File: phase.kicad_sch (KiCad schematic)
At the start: 19 parts

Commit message: finished schematics
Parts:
- removed U?: BSC040N08, Package_TO_SOT_SMD:LFPAK56_ThermalVias-1, symbol Transistor_FET:BSC040N08NS5
- removed U?: 22R, Resistor_SMD:R_0603_1608Metric, symbol Device:R
- removed U?: 0mr5, Resistor_SMD:R_2512_6332Metric, symbol Device:R
- removed U?: 10u, Capacitor_SMD:C_2220_5650Metric, symbol Device:C
- added C39: 10u, Capacitor_SMD:C_2220_5650Metric, symbol Device:C
- added Q24: BSC040N08, Package_TO_SOT_SMD:TDSON-8-1, symbol Transistor_FET:BSC040N08NS5
- added R31: 22R, Resistor_SMD:R_0603_1608Metric, symbol Device:R
- added R34: 0mr5, Resistor_SMD:R_2512_6332Metric, symbol Device:R
- Q23: renamed from U?; footprint Package_TO_SOT_SMD:LFPAK56_ThermalVias-1 -> Package_TO_SOT_SMD:TDSON-8-1
- gave numbers to parts that had none: 14
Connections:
- net GND is gone; now on net GNDA: C40.2, U25.1 (GND), U25.4 (GND), U25.7 (REF1)
- net +BATT: now also C39.1
- net GNDPWR: now also C39.2, Q24.1 (S), Q24.2 (S), Q24.3 (S)
- net Phase: now also R34.1
- net at C34.2, C35.2, Q23.1 (S)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: now also R32.1, Q24.5 (D), R34.2
- net at U24.5 (LO): now also R31.2
- net V: now reaches C36.1, R32.2, R33.1
- net +3.3VA renamed +3.3VADC
- new net: Q24.4 (G), R31.1
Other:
- company: (none) -> UNIMOC universal motor controller
- title: Phase -> (BCC) Battery Case Controller

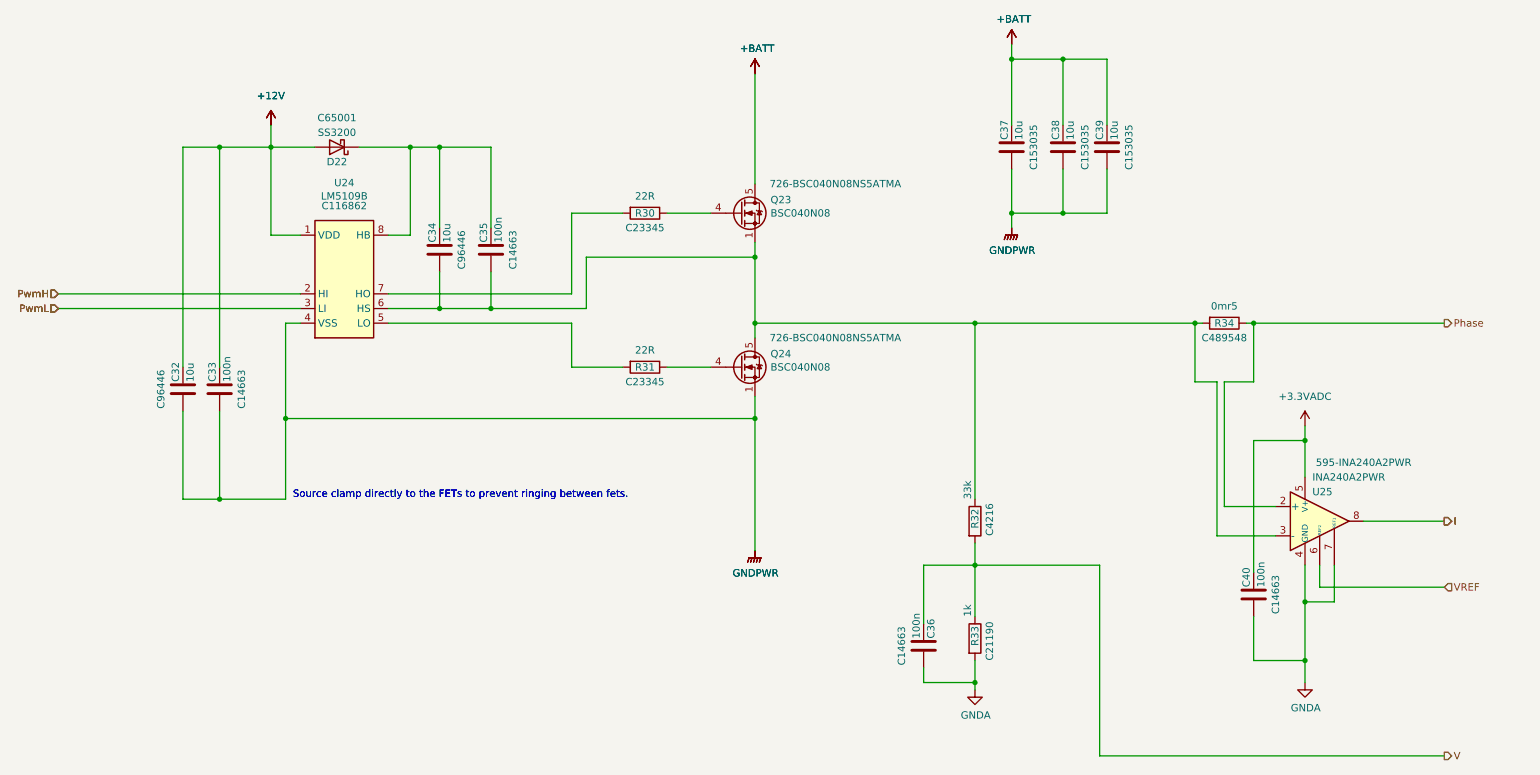
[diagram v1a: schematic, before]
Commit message: Placing first round finished
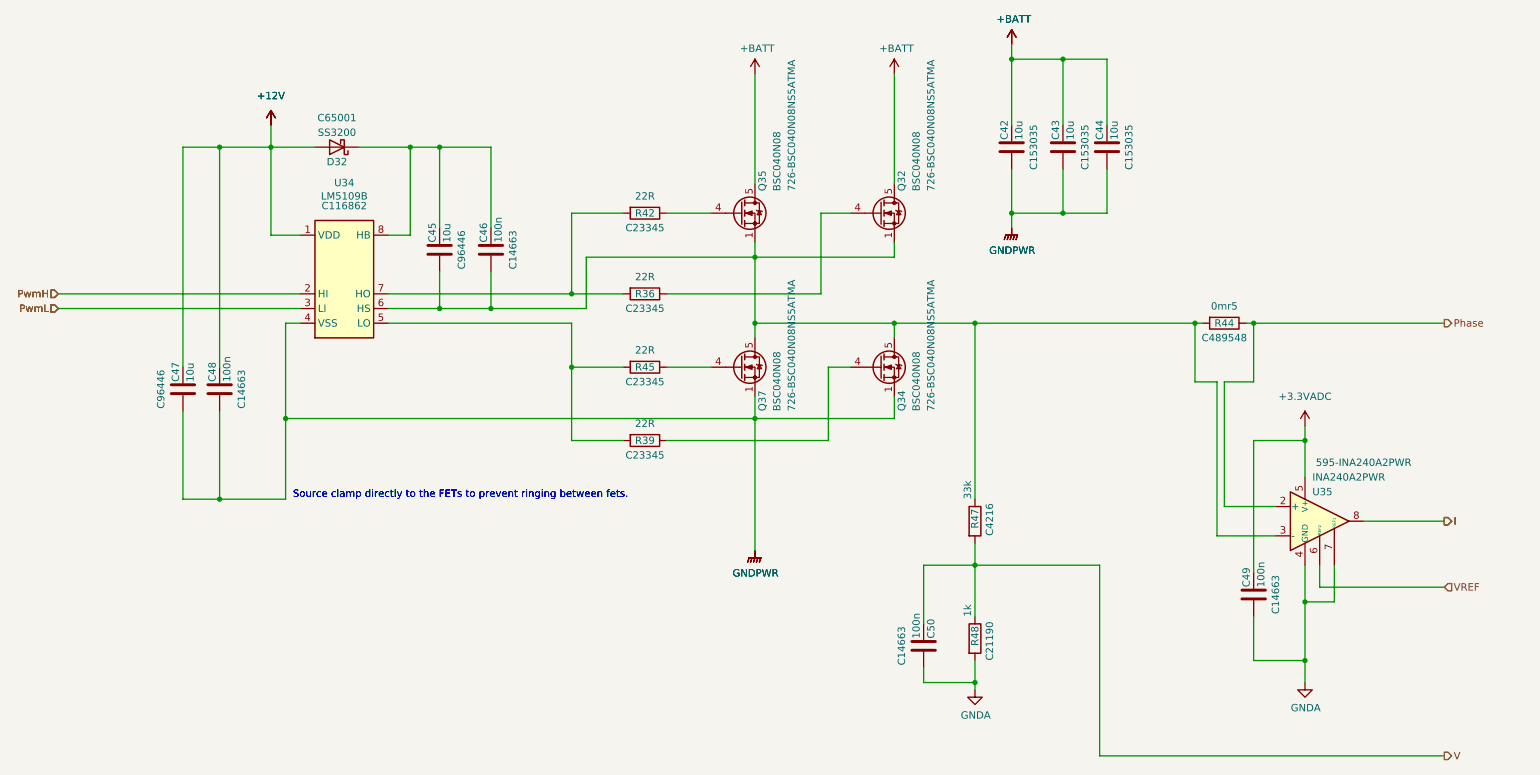
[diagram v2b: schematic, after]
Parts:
- added Q32, Q34: BSC040N08, Package_TO_SOT_SMD:TDSON-8-1, symbol Transistor_FET:BSC040N08NS5
- added R36, R39: 22R, Resistor_SMD:R_0603_1608Metric, symbol Device:R
- renumbered C37 to C42, C38 to C43, C39 to C44, C34 to C45, C35 to C46, C32 to C47, C33 to C48, C40 to C49, C36 to C50, D22 to D32, Q23 to Q35, Q24 to Q37, R30 to R42, R34 to R44, R31 to R45, R32 to R47, R33 to R48, U24 to U34, U25 to U35
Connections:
- net +BATT: now also Q32.5 (D)
- net GNDPWR: now also Q34.1 (S), Q34.2 (S), Q34.3 (S)
- net at C45.2, C46.2, Q35.1 (S)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: now also Q32.1 (S), Q32.2 (S), Q32.3 (S), Q34.5 (D)
- net at R42.2, U34.7 (HO): now also R36.2
- net at R45.2, U34.5 (LO): now also R39.2
- new net: Q34.4 (G), R39.1
- new net: Q32.4 (G), R36.1

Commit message: just the silk open
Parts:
- added C41: 100n, Capacitor_SMD:C_0603_1608Metric, symbol Device:C
- added C42: 2n2, Capacitor_SMD:C_0603_1608Metric, symbol Device:C
- added R41: 1k, Resistor_SMD:R_0603_1608Metric, symbol Device:R
- renumbered C42 to C44, C43 to C45, C44 to C46, C45 to C47, C46 to C48, C47 to C49, C48 to C50, C49 to C51, C50 to C54, Q32 to Q36, Q34 to Q38, R42 to R43, R36 to R44, R44 to R45, R45 to R46, R39 to R47, R47 to R48, R48 to R50
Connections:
- net GNDA: now also C41.2, C42.2
- net I: now also C42.1, R41.2; no longer U35.8
- net VREF: now also C41.1
- new net: R41.1, U35.8

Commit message: Fixed pinning error for Display RX and PWM Break
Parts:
- renumbered C41 to C52, C42 to C53, R41 to R49
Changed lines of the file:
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@@
   (symbol (lib_id "Device:C") (at 250.19 119.38 0) (unit 1)
     (in_bom yes) (on_board yes)
-    (property "Reference" "C41" (id 0) (at 248.92 118.11 90)
+    (property "Reference" "C52" (id 0) (at 248.92 118.11 90)
       (effects (font (size 1.27 1.27)) (justify left))
     )
@@
   (symbol (lib_id "Device:C") (at 266.7 119.38 0) (unit 1)
     (in_bom yes) (on_board yes)
-    (property "Reference" "C42" (id 0) (at 265.43 118.11 90)
+    (property "Reference" "C53" (id 0) (at 265.43 118.11 90)
       (effects (font (size 1.27 1.27)) (justify left))
     )
@@
   (symbol (lib_id "Device:R") (at 259.08 101.6 90) (unit 1)
     (in_bom yes) (on_board yes)
-    (property "Reference" "R41" (id 0) (at 260.35 101.6 90)
-      (effects (font (size 1.27 1.27)) (justify left))
-    )
+    (property "Reference" "R49" (id 0) (at 260.35 101.6 90)
+      (effects (font (size 1.27 1.27)) (justify left))
+    )

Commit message: added Pulldowns to the PWM wires
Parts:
- added R90, R91: 10k, Resistor_SMD:R_0603_1608Metric, symbol Device:R
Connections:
- net GNDPWR: now also R90.2, R91.2
- net PwmH: now also R91.1
- net PwmL: now also R90.1
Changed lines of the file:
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@@
   (junction (at 91.44 36.83) (diameter 0) (color 0 0 0 0)
   )
+  (junction (at 31.75 64.77) (diameter 0) (color 0 0 0 0)
+  )
   (junction (at 146.05 55.88) (diameter 0) (color 0 0 0 0)
   )
+  (junction (at 36.83 62.23) (diameter 0) (color 0 0 0 0)
+  )
   (junction (at 184.15 129.54) (diameter 0) (color 0 0 0 0)
   )
   (junction (at 114.3 62.23) (diameter 0) (color 0 0 0 0)
   )
+  (junction (at 36.83 97.79) (diameter 0) (color 0 0 0 0)
+  )
+  (junction (at 46.99 97.79) (diameter 0) (color 0 0 0 0)
+  )
   (junction (at 222.25 67.31) (diameter 0) (color 0 0 0 0)
   )
@@
   (junction (at 100.33 64.77) (diameter 0) (color 0 0 0 0)
   )
+  (wire (pts (xy 36.83 97.79) (xy 46.99 97.79))
+    (stroke (width 0) (type default) (color 0 0 0 0))
+  )
   (wire (pts (xy 67.31 52.07) (xy 62.23 52.07))
     (stroke (width 0) (type default) (color 0 0 0 0))
@@
     (stroke (width 0) (type default) (color 0 0 0 0))
   )
+  (wire (pts (xy 31.75 64.77) (xy 31.75 74.93))
+    (stroke (width 0) (type default) (color 0 0 0 0))
+  )
   (wire (pts (xy 64.77 97.79) (xy 53.34 97.79))
     (stroke (width 0) (type default) (color 0 0 0 0))
@@
     (stroke (width 0) (type default) (color 0 0 0 0))
   )
+  (wire (pts (xy 36.83 82.55) (xy 36.83 97.79))
+    (stroke (width 0) (type default) (color 0 0 0 0))
+  )
   (wire (pts (xy 91.44 64.77) (xy 91.44 58.42))
     (stroke (width 0) (type default) (color 0 0 0 0))
@@
     (stroke (width 0) (type default) (color 0 0 0 0))
   )
-  (wire (pts (xy 25.4 64.77) (xy 67.31 64.77))
+  (wire (pts (xy 25.4 64.77) (xy 31.75 64.77))
+    (stroke (width 0) (type default) (color 0 0 0 0))
+  )
+  (wire (pts (xy 31.75 97.79) (xy 36.83 97.79))
     (stroke (width 0) (type default) (color 0 0 0 0))
   )
@@
     (stroke (width 0) (type default) (color 0 0 0 0))
   )
+  (wire (pts (xy 31.75 82.55) (xy 31.75 97.79))
+    (stroke (width 0) (type default) (color 0 0 0 0))
+  )
   (wire (pts (xy 262.89 101.6) (xy 266.7 101.6))
     (stroke (width 0) (type default) (color 0 0 0 0))
@@
     (stroke (width 0) (type default) (color 0 0 0 0))
   )
+  (wire (pts (xy 36.83 62.23) (xy 67.31 62.23))
+    (stroke (width 0) (type default) (color 0 0 0 0))
+  )
   (wire (pts (xy 114.3 87.63) (xy 114.3 74.93))
     (stroke (width 0) (type default) (color 0 0 0 0))
@@
     (stroke (width 0) (type default) (color 0 0 0 0))
   )
-  (wire (pts (xy 25.4 62.23) (xy 67.31 62.23))
+  (wire (pts (xy 25.4 62.23) (xy 36.83 62.23))
     (stroke (width 0) (type default) (color 0 0 0 0))
   )
@@
     (stroke (width 0) (type default) (color 0 0 0 0))
   )
+  (wire (pts (xy 31.75 64.77) (xy 67.31 64.77))
+    (stroke (width 0) (type default) (color 0 0 0 0))
+  )
   (wire (pts (xy 184.15 67.31) (xy 222.25 67.31))
     (stroke (width 0) (type default) (color 0 0 0 0))
@@
   )
   (wire (pts (xy 170.18 55.88) (xy 170.18 53.34))
+    (stroke (width 0) (type default) (color 0 0 0 0))
+  )
+  (wire (pts (xy 36.83 62.23) (xy 36.83 74.93))
     (stroke (width 0) (type default) (color 0 0 0 0))
   )
@@
     (pin "5")
   )
+  (symbol (lib_id "Device:R") (at 36.83 78.74 0) (unit 1)
+    (in_bom yes) (on_board yes)
+    (property "Reference" "R91" (id 0) (at 36.83 80.01 90)
+      (effects (font (size 1.27 1.27)) (justify left))
+    )
+    (property "Value" "10k" (id 1) (at 35.56 76.2 90)
+      (effects (font (size 1.27 1.27)) (justify left))
+    )
+    (property "Footprint" "Resistor_SMD:R_0603_1608Metric" (id 2) (at 35.052 78.74 90)
+      (effects (font (size 1.27 1.27)) hide)
+    )
+    (property "Datasheet" "~" (id 3) (at 36.83 78.74 0)
+      (effects (font (size 1.27 1.27)) hide)
+    )
+    (property "LCSC#" "C25804" (id 4) (at 38.1 76.2 90)
+      (effects (font (size 1.27 1.27)) (justify left))
+    )
+    (pin "1")
+    (pin "2")
+  )
   (symbol (lib_id "power:GNDA") (at 184.15 130.81 0) (unit 1)
     (in_bom yes) (on_board yes)
@@
     (pin "5")
   )
+  (symbol (lib_id "Device:R") (at 31.75 78.74 0) (unit 1)
+    (in_bom yes) (on_board yes)
+    (property "Reference" "R90" (id 0) (at 31.75 80.01 90)
+      (effects (font (size 1.27 1.27)) (justify left))
+    )
+    (property "Value" "10k" (id 1) (at 30.48 76.2 90)
+      (effects (font (size 1.27 1.27)) (justify left))
+    )
+    (property "Footprint" "Resistor_SMD:R_0603_1608Metric" (id 2) (at 29.972 78.74 90)
+      (effects (font (size 1.27 1.27)) hide)
+    )
+    (property "Datasheet" "~" (id 3) (at 31.75 78.74 0)
+      (effects (font (size 1.27 1.27)) hide)
+    )
+    (property "LCSC#" "C25804" (id 4) (at 33.02 76.2 90)
+      (effects (font (size 1.27 1.27)) (justify left))
+    )
+    (pin "1")
+    (pin "2")
+  )
   (symbol (lib_id "power:+BATT") (at 146.05 24.13 0) (unit 1)
